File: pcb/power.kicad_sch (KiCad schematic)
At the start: 1 part, among them J3 Power

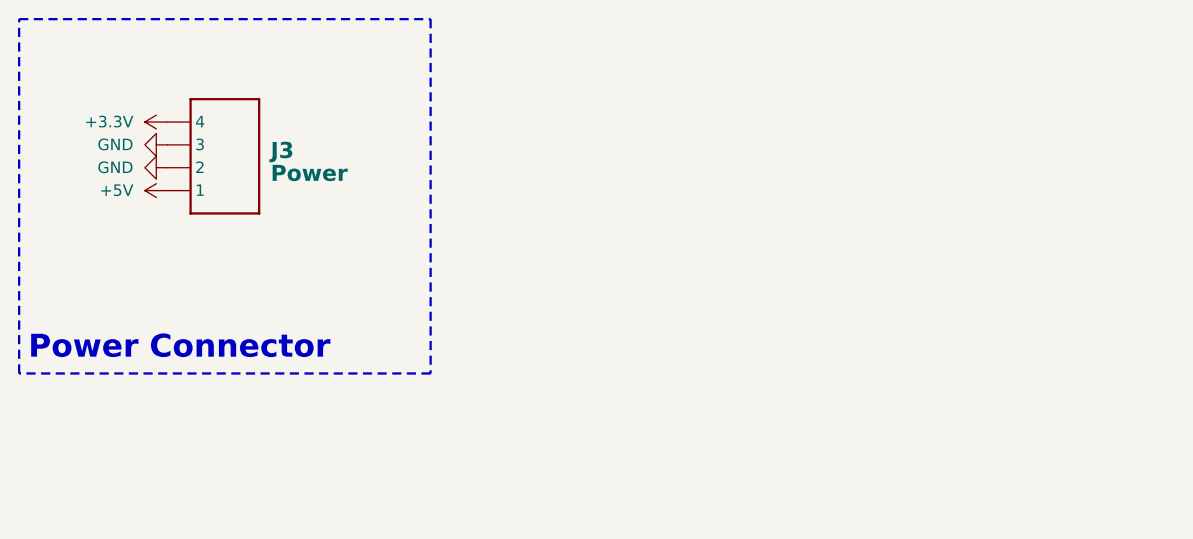
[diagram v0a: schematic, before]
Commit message: Reworked based on new standards
Decreased to 3 servo ports
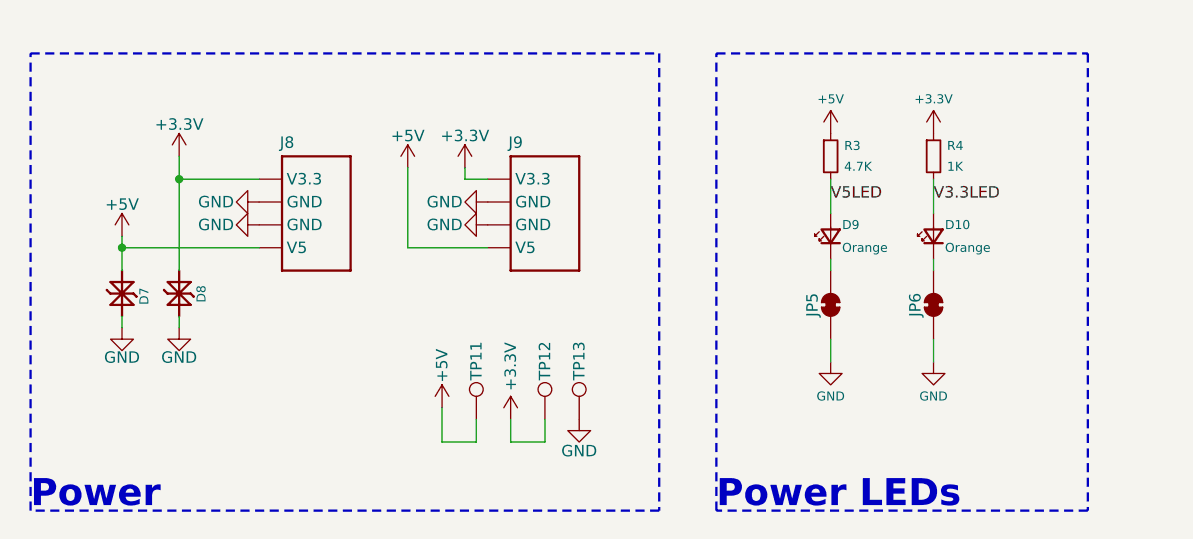
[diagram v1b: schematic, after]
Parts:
- removed J3: Power, Connector_JST:JST_SH_SM04B-SRSS-TB_1x04-1MP_P1.00mm_Horizontal, symbol CRGM Connector:JST-SH-4
- added D10, D9: Orange, CRGM Passive:LED_0603_1608Metric, symbol Device:LED_Small
- added D7: PESD5V5C1BL, CRGM Passive:DFN1006-2, symbol CRGM Passive:PESD5V5C1BLYL
- added D8: PESD3V3S1BL, CRGM Passive:DFN1006-2, symbol CRGM Passive:PESD3V3S1BL
- added J8, J9: ~, CRGM Connector:JST_SH_SM04B-SRSS-TB_1x04-1MP_P1.00mm_Horizontal, symbol CRGM Connector:AQ_POWER
- added JP5, JP6: ~, CRGM Connector:SolderJumper-2_P1.3mm_Bridged_RoundedPad1.0x1.5mm, symbol Jumper:SolderJumper_2_Bridged
- added R3: 4.7K, CRGM Passive:R_0603_1608Metric, symbol Device:R_Small
- added R4: 1K, CRGM Passive:R_0603_1608Metric, symbol Device:R_Small
- added TP11, TP12, TP13: ~, CRGM Mechanical:TestPoint_Pad_D1.0mm, symbol CRGM Connector:TestPoint
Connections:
- net +3.3V: now also D8.2 (K2), J8.4 (V3.3), J9.4 (V3.3), R4.1, TP12.1
- net +5V: now also D7.2 (K2), J8.1 (V5), J9.1 (V5), R3.1, TP11.1
- net GND: now also D7.1 (K1), D8.1 (K1), J8.2 (GND), J8.3 (GND), J9.2 (GND), J9.3 (GND), JP5.1 (A), JP6.1 (A), TP13.1
- new net: D10.1 (K), JP6.2 (B)
- new net: D9.1 (K), JP5.2 (B)
- new net V3.3LED: D10.2 (A), R4.2
- new net V5LED: D9.2 (A), R3.2
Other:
- note added: "Power"
- note added: "Power LEDs"
- note removed: "Power Connector"

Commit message: Added status leds
forced to reroute entire board
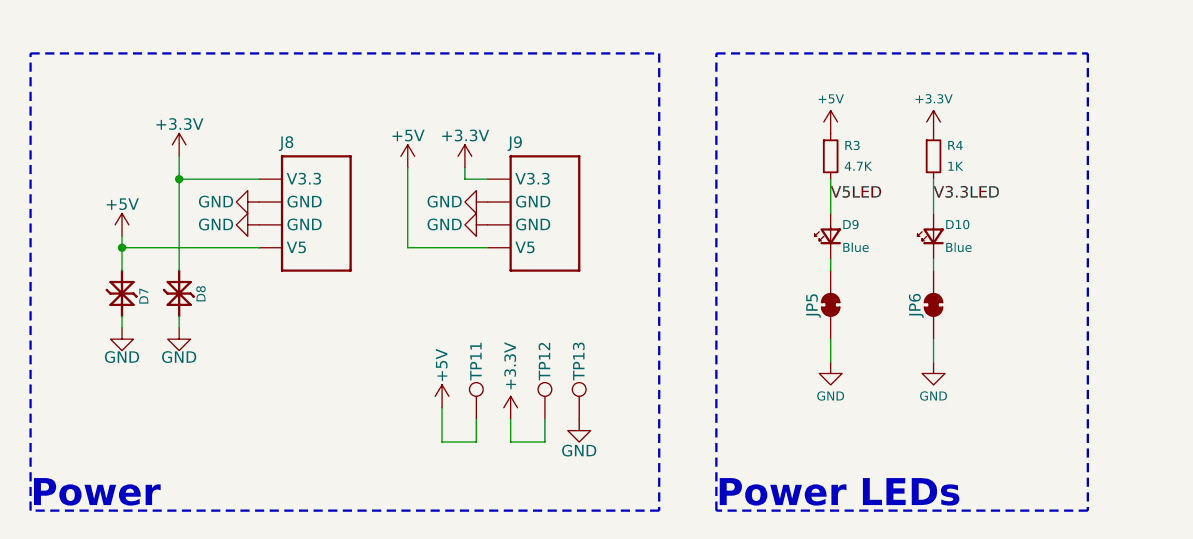
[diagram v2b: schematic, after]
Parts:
- D10, D9: value Orange -> Blue; Digikey 5962-XL-1608UOC-06TR-ND -> 5962-XL-1608UBC-04TR-ND; LCSC C965800 -> C965807; MPN XL-1608UOC-06 -> XL-1608UBC-04; Mouser 859-LTST-C190KFKT -> 859-LTST-C190TBKT
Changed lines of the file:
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@@
 			)
 		)
-		(property "Value" "Orange"
+		(property "Value" "Blue"
 			(at 115.57 46.99 90)
 			(effects
@@
 			)
 		)
-		(property "Datasheet" "https://optoelectronics.liteon.com/upload/download/DS22-2000-228/LTST-C191KGKT.PDF"
+		(property "Datasheet" "https://optoelectronics.liteon.com/upload/download/DS-22-99-0224/LTST-C190TBKT.PDF"
 			(at 114.3 45.72 0)
 			(effects
@@
 			)
 		)
-		(property "Description" "20mA 315mcd Colorless Orange 120° 50mW 2.3V 0603"
+		(property "Description" "Blue 120° 3.3V 300mcd 470nm 70mW 0603"
 			(at 114.3 45.72 0)
 			(effects
@@
 			)
 		)
-		(property "MPN" "XL-1608UOC-06"
+		(property "MPN" "XL-1608UBC-04"
 			(at 114.3 45.72 0)
 			(effects
@@
 			)
 		)
-		(property "Mouser" "859-LTST-C190KFKT"
+		(property "Mouser" "859-LTST-C190TBKT"
 			(at 114.3 45.72 0)
 			(effects
@@
 			)
 		)
-		(property "Digikey" "5962-XL-1608UOC-06TR-ND"
+		(property "Digikey" "5962-XL-1608UBC-04TR-ND"
 			(at 114.3 45.72 0)
 			(effects
@@
 			)
 		)
-		(property "LCSC" "C965800"
+		(property "LCSC" "C965807"
 			(at 114.3 45.72 0)
 			(effects
@@
 					(size 1 1)
 					(color 223 129 255 1)
-				)
-				(hide yes)
-			)
-		)
-		(property "ALT_LCSC" ""
-			(at 114.3 45.72 90)
-			(effects
-				(font
-					(size 1.27 1.27)
-				)
-				(hide yes)
-			)
-		)
-		(property "ALT_LCSC_2" ""
-			(at 114.3 45.72 90)
-			(effects
-				(font
-					(size 1.27 1.27)
-				)
-				(hide yes)
-			)
-		)
-		(property "ALT_MN" ""
-			(at 114.3 45.72 90)
-			(effects
-				(font
-					(size 1.27 1.27)
-				)
-				(hide yes)
-			)
-		)
-		(property "ALT_MPN" ""
-			(at 114.3 45.72 90)
-			(effects
-				(font
-					(size 1.27 1.27)
 				)
 				(hide yes)
@@
 	)
 	(symbol
-		(lib_id "Device:LED_Small")
-		(at 125.73 45.72 90)
-		(unit 1)
-		(exclude_from_sim no)
-		(in_bom yes)
-		(on_board yes)
-		(dnp no)
-		(property "Reference" "D10"
-			(at 127 44.45 90)
-			(effects
-				(font
-					(size 1 1)
-				)
-				(justify right)
-			)
-		)
-		(property "Value" "Orange"
-			(at 127 46.99 90)
-			(effects
-				(font
-					(size 1 1)
-				)
-				(justify right)
-			)
-		)
-		(property "Footprint" "CRGM Passive:LED_0603_1608Metric"
-			(at 125.73 45.72 0)
-			(effects
-				(font
-					(size 1 1)
-					(color 223 129 255 1)
-				)
-				(hide yes)
-			)
-		)
-		(property "Datasheet" "https://optoelectronics.liteon.com/upload/download/DS22-2000-228/LTST-C191KGKT.PDF"
-			(at 125.73 45.72 0)
-			(effects
-				(font
-					(size 1 1)
-					(color 223 129 255 1)
-				)
-				(hide yes)
-			)
-		)
-		(property "Description" "20mA 315mcd Colorless Orange 120° 50mW 2.3V 0603"
-			(at 125.73 45.72 0)
-			(effects
-				(font
-					(size 1.27 1.27)
-				)
-				(hide yes)
-			)
-		)
-		(property "MN" "XINGLIGHT"
-			(at 125.73 45.72 0)
-			(effects
-				(font
-					(size 1.27 1.27)
-				)
-				(hide yes)
-			)
-		)
-		(property "MPN" "XL-1608UOC-06"
-			(at 125.73 45.72 0)
-			(effects
-				(font
-					(size 1.27 1.27)
-				)
-				(hide yes)
-			)
-		)
-		(property "Mouser" "859-LTST-C190KFKT"
-			(at 125.73 45.72 0)
-			(effects
-				(font
-					(size 1 1)
-					(color 223 129 255 1)
-				)
-				(hide yes)
-			)
-		)
-		(property "Digikey" "5962-XL-1608UOC-06TR-ND"
-			(at 125.73 45.72 0)
-			(effects
-				(font
-					(size 1 1)
-					(color 223 129 255 1)
-				)
-				(hide yes)
-			)
-		)
-		(property "LCSC" "C965800"
-			(at 125.73 45.72 0)
-			(effects
-				(font
-					(size 1 1)
-					(color 223 129 255 1)
-				)
-				(hide yes)
-			)
-		)
-		(property "ALT_LCSC" ""
-			(at 125.73 45.72 90)
-			(effects
-				(font
-					(size 1.27 1.27)
-				)
-				(hide yes)
-			)
-		)
-		(property "ALT_LCSC_2" ""
-			(at 125.73 45.72 90)
-			(effects
-				(font
-					(size 1.27 1.27)
-				)
-				(hide yes)
-			)
-		)
-		(property "ALT_MN" ""
-			(at 125.73 45.72 90)
-			(effects
-				(font
-					(size 1.27 1.27)
-				)
-				(hide yes)
-			)
-		)
-		(property "ALT_MPN" ""
-			(at 125.73 45.72 90)
-			(effects
-				(font
-					(size 1.27 1.27)
-				)
-				(hide yes)
-			)
-		)
-		(pin "1"
-		)
-		(pin "2"
-		)
-		(instances
-			(project "servo-module"
-				(path "/445c1fff-2e1a-48b1-a91f-a137832edebf/eeaa896c-88e5-4042-8d3a-e7c6f02bca2a"
-					(reference "D10")
-					(unit 1)
-				)
-			)
-		)
-	)
-	(symbol
 		(lib_id "power:+3.3V")
 		(at 125.73 34.29 0)
@@
 					(unit 1)
 				)
+			)
+		)
+	)
+	(symbol
+		(lib_id "Device:LED_Small")
+		(at 125.73 45.72 90)
+		(unit 1)
+		(exclude_from_sim no)
+		(in_bom yes)
+		(on_board yes)
+		(dnp no)
+		(property "Reference" "D10"
+			(at 127 44.45 90)
+			(effects
+				(font
+					(size 1 1)
+				)
+				(justify right)
+			)
+		)
+		(property "Value" "Blue"
+			(at 127 46.99 90)
+			(effects
+				(font
+					(size 1 1)
+				)
+				(justify right)
+			)
+		)
+		(property "Footprint" "CRGM Passive:LED_0603_1608Metric"
+			(at 125.73 45.72 0)
+			(effects
+				(font
+					(size 1 1)
+					(color 223 129 255 1)
+				)
+				(hide yes)
+			)
+		)
+		(property "Datasheet" "https://optoelectronics.liteon.com/upload/download/DS-22-99-0224/LTST-C190TBKT.PDF"
+			(at 125.73 45.72 0)
+			(effects
+				(font
+					(size 1 1)
+					(color 223 129 255 1)
+				)
+				(hide yes)
+			)
+		)
+		(property "Description" "Blue 120° 3.3V 300mcd 470nm 70mW 0603"
+			(at 125.73 45.72 0)
+			(effects
+				(font
+					(size 1.27 1.27)
+				)
+				(hide yes)
+			)
+		)
+		(property "MN" "XINGLIGHT"
+			(at 125.73 45.72 0)
+			(effects
+				(font
+					(size 1.27 1.27)
+				)
+				(hide yes)
+			)
+		)
+		(property "MPN" "XL-1608UBC-04"
+			(at 125.73 45.72 0)
+			(effects
+				(font
+					(size 1.27 1.27)
+				)
+				(hide yes)
+			)
+		)
+		(property "Mouser" "859-LTST-C190TBKT"
+			(at 125.73 45.72 0)
+			(effects
+				(font
+					(size 1 1)
+					(color 223 129 255 1)
+				)
+				(hide yes)
+			)
+		)
+		(property "Digikey" "5962-XL-1608UBC-04TR-ND"
+			(at 125.73 45.72 0)
+			(effects
+				(font
+					(size 1 1)
+					(color 223 129 255 1)
+				)
+				(hide yes)
+			)
+		)
+		(property "LCSC" "C965807"
+			(at 125.73 45.72 0)
+			(effects
+				(font
+					(size 1 1)
+					(color 223 129 255 1)
+				)
+				(hide yes)
+			)
+		)
+		(pin "1"
+		)
+		(pin "2"
+		)
+		(instances
+			(project "servo-module"
+				(path "/445c1fff-2e1a-48b1-a91f-a137832edebf/eeaa896c-88e5-4042-8d3a-e7c6f02bca2a"
+					(reference "D10")
+					(unit 1)
+				)

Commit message: Added servo power and filtering
Added connection for servo power
Added solder jumper for servo power to 5V
Added caps to servo power
Added bulk decoupling caps
Added TVS to various inputs
Updated renders
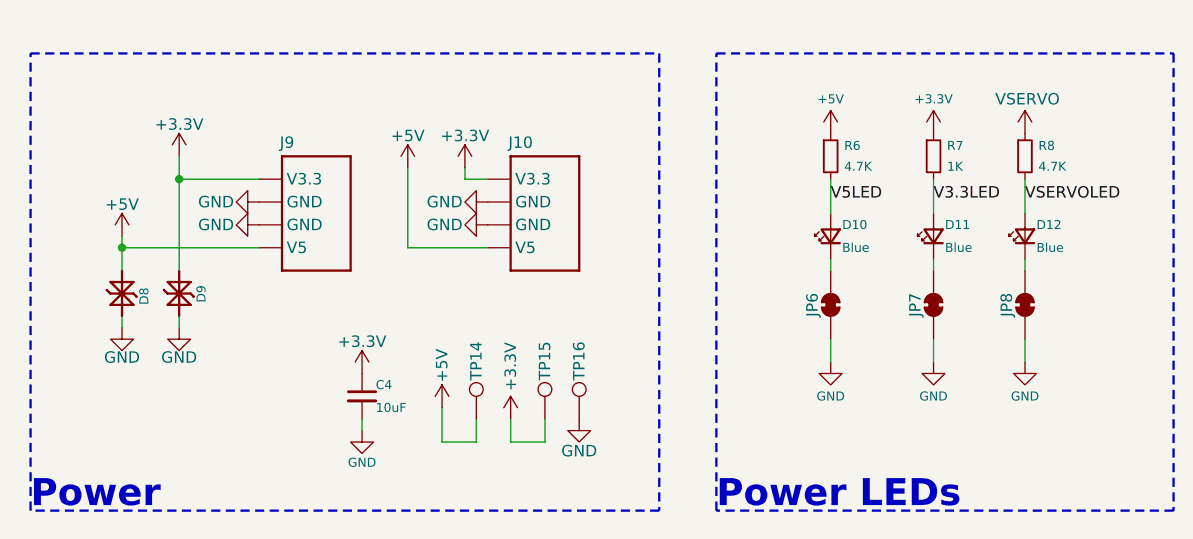
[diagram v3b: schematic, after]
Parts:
- added C4: 10uF, CRGM Passive:C_0603_1608Metric, symbol Device:C_Small
- added D12: Blue, CRGM Passive:LED_0603_1608Metric, symbol Device:LED_Small
- added JP8: ~, CRGM Connector:SolderJumper-2_P1.3mm_Bridged_RoundedPad1.0x1.5mm, symbol Jumper:SolderJumper_2_Bridged
- added R8: 4.7K, CRGM Passive:R_0603_1608Metric, symbol Device:R_Small
- renumbered D9 to D10, D10 to D11, D7 to D8, D8 to D9, J9 to J10, J8 to J9, JP5 to JP6, JP6 to JP7, R3 to R6, R4 to R7, TP11 to TP14, TP12 to TP15, TP13 to TP16
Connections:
- net +3.3V: now also C4.1
- net GND: now also C4.2, JP8.1 (A)
- new net: D12.1 (K), JP8.2 (B)
- new net VSERVO: R8.1
- new net VSERVOLED: D12.2 (A), R8.2

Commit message: Updated title; deleted unnecessary files
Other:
- title: Relay Module -> Servo Module
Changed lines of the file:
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@@
 	(paper "A4")
 	(title_block
-		(title "Relay Module")
+		(title "Servo Module")
 		(date "2025-03-22")
 		(rev "1.0")

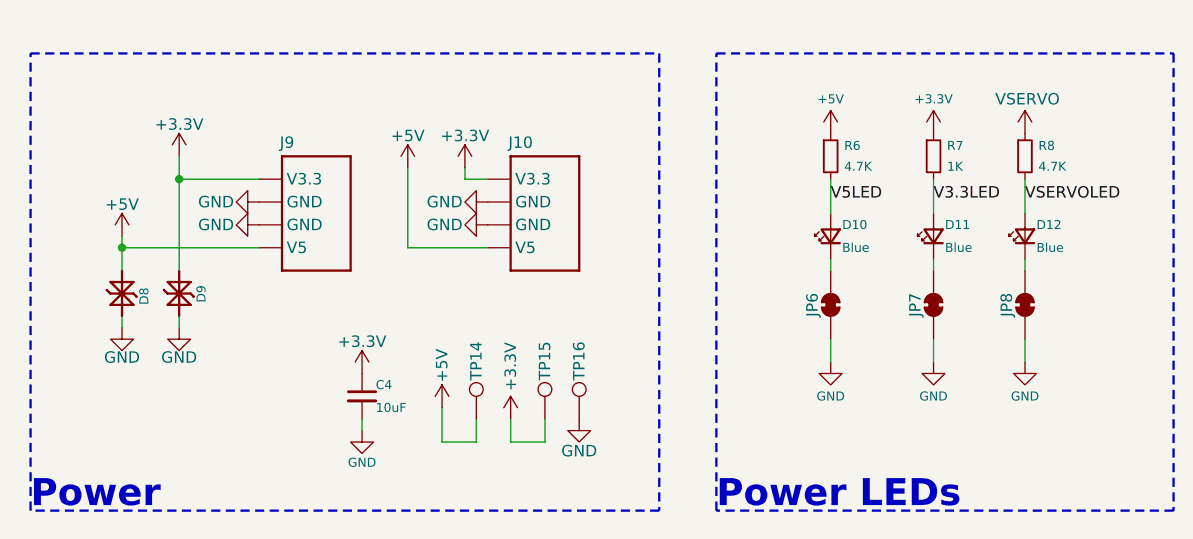
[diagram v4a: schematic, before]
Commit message: changed connectors to vertical
Updated connectors with ground on mounting points
Updated and rerouted
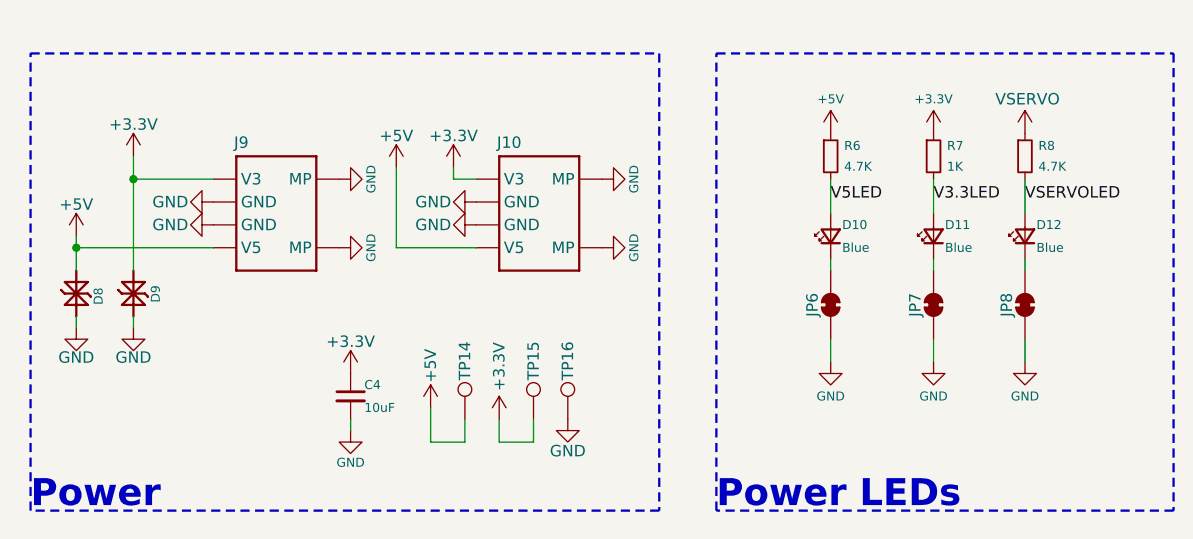
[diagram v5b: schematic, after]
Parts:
- J10, J9: footprint CRGM Connector:JST_SH_SM04B-SRSS-TB_1x04-1MP_P1.00mm_Horizontal -> CRGM Connector:JST_SH_BM04B-SRSS-TB_1x04-1MP_P1.00mm_Vertical; Digikey 455-SM04B-SRSS-TBTR-ND -> 455-SBM04B-SRSS-TBTR-ND; LCSC C2763614 -> C2904986; MPN SM04B-SRSS-TBT(LF)(SN) -> BM04B-SRSS-TBT(LF)(SN); Mouser 306-SM04BSRSSTBTLFSN -> 306-BM04B-SRSS-TBTLFSN
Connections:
- net GND: now also J10.0 (MP), J10.5 (MP), J9.0 (MP), J9.5 (MP)
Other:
- moved on the sheet: C4, D8, D9, TP14, TP15, TP16

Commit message: Removed space in MN for resistors
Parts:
- R6, R8: MN FOJAN -> FOJAN
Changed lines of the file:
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@@
 			)
 		)
-		(property "MN" "FOJAN "
+		(property "MN" "FOJAN"
 			(at 135.89 36.83 0)
 			(effects
@@
 			)
 		)
-		(property "MN" "FOJAN "
+		(property "MN" "FOJAN"
 			(at 114.3 36.83 0)
 			(effects

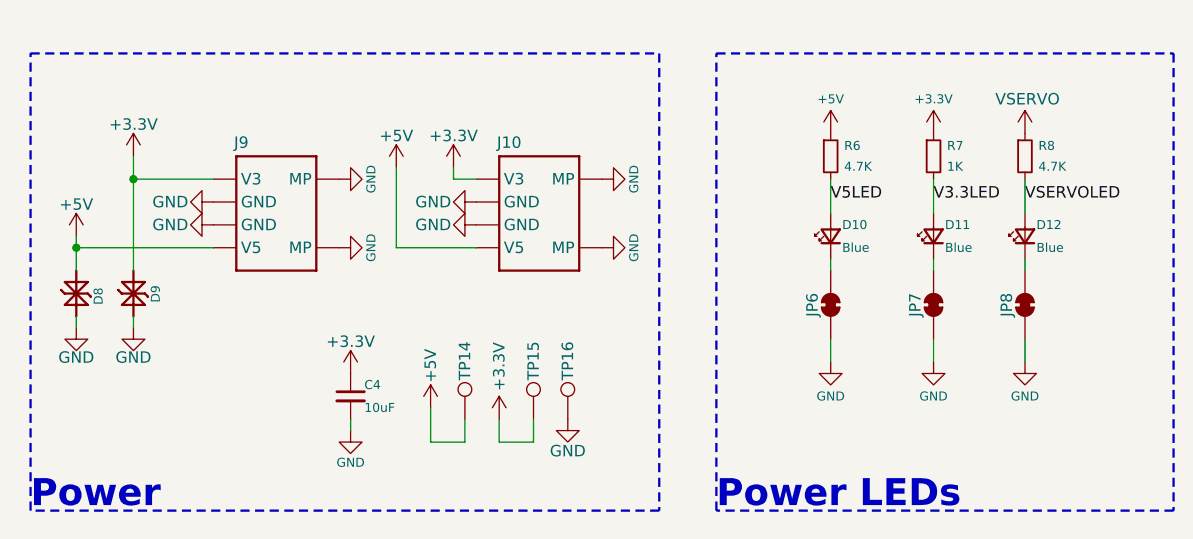
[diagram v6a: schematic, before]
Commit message: Redesign with SMT32
Complete redesign using SMT32 instead of ATTINY.
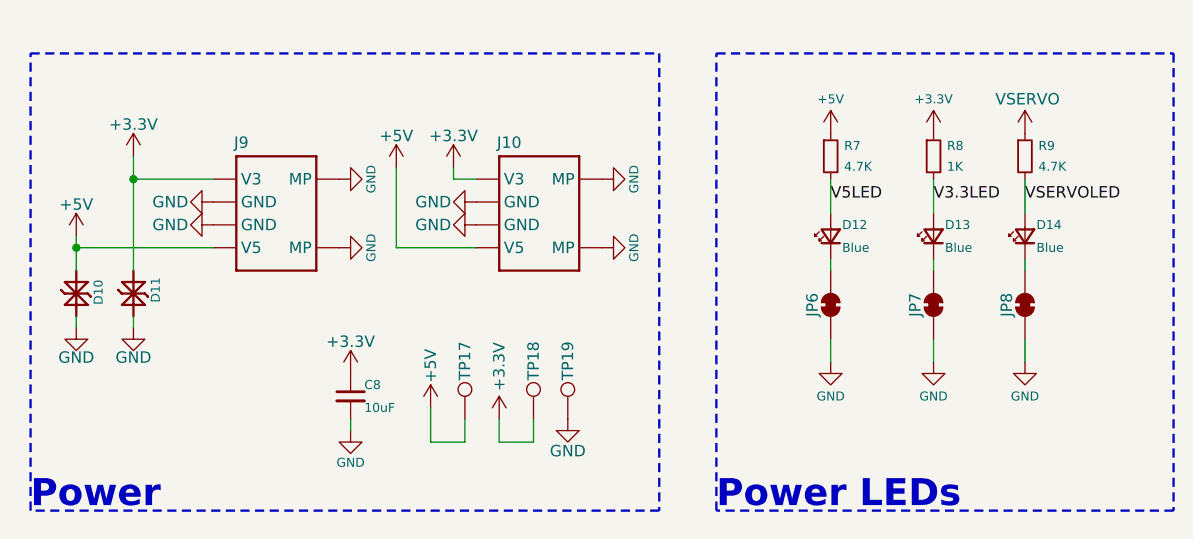
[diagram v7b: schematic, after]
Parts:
- R7: renamed from R6; MN FOJAN -> FOJAN
- R9: renamed from R8; MN FOJAN -> FOJAN
- renumbered C4 to C8, D8 to D10, D9 to D11, D10 to D12, D11 to D13, D12 to D14, R7 to R8, TP14 to TP17, TP15 to TP18, TP16 to TP19

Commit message: removed space
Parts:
- R7, R9: MN FOJAN -> FOJAN
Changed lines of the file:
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@@
 			)
 		)
-		(property "MN" "FOJAN "
+		(property "MN" "FOJAN"
 			(at 135.89 36.83 0)
 			(effects
@@
 			)
 		)
-		(property "MN" "FOJAN "
+		(property "MN" "FOJAN"
 			(at 114.3 36.83 0)
 			(effects
